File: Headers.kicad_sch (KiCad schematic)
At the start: 17 parts, among them J1 Conn_01x06_Pin, J10 Conn_01x03_Pin, J11 Conn_02x05_Odd_Even, J17 Conn_01x01_Pin, J18 Conn_02x05_Odd_Even, J2 Conn_01x06_Pin, J21 Conn_01x02_Pin, J5 Conn_01x02_Pin, J8 Conn_01x03_Pin

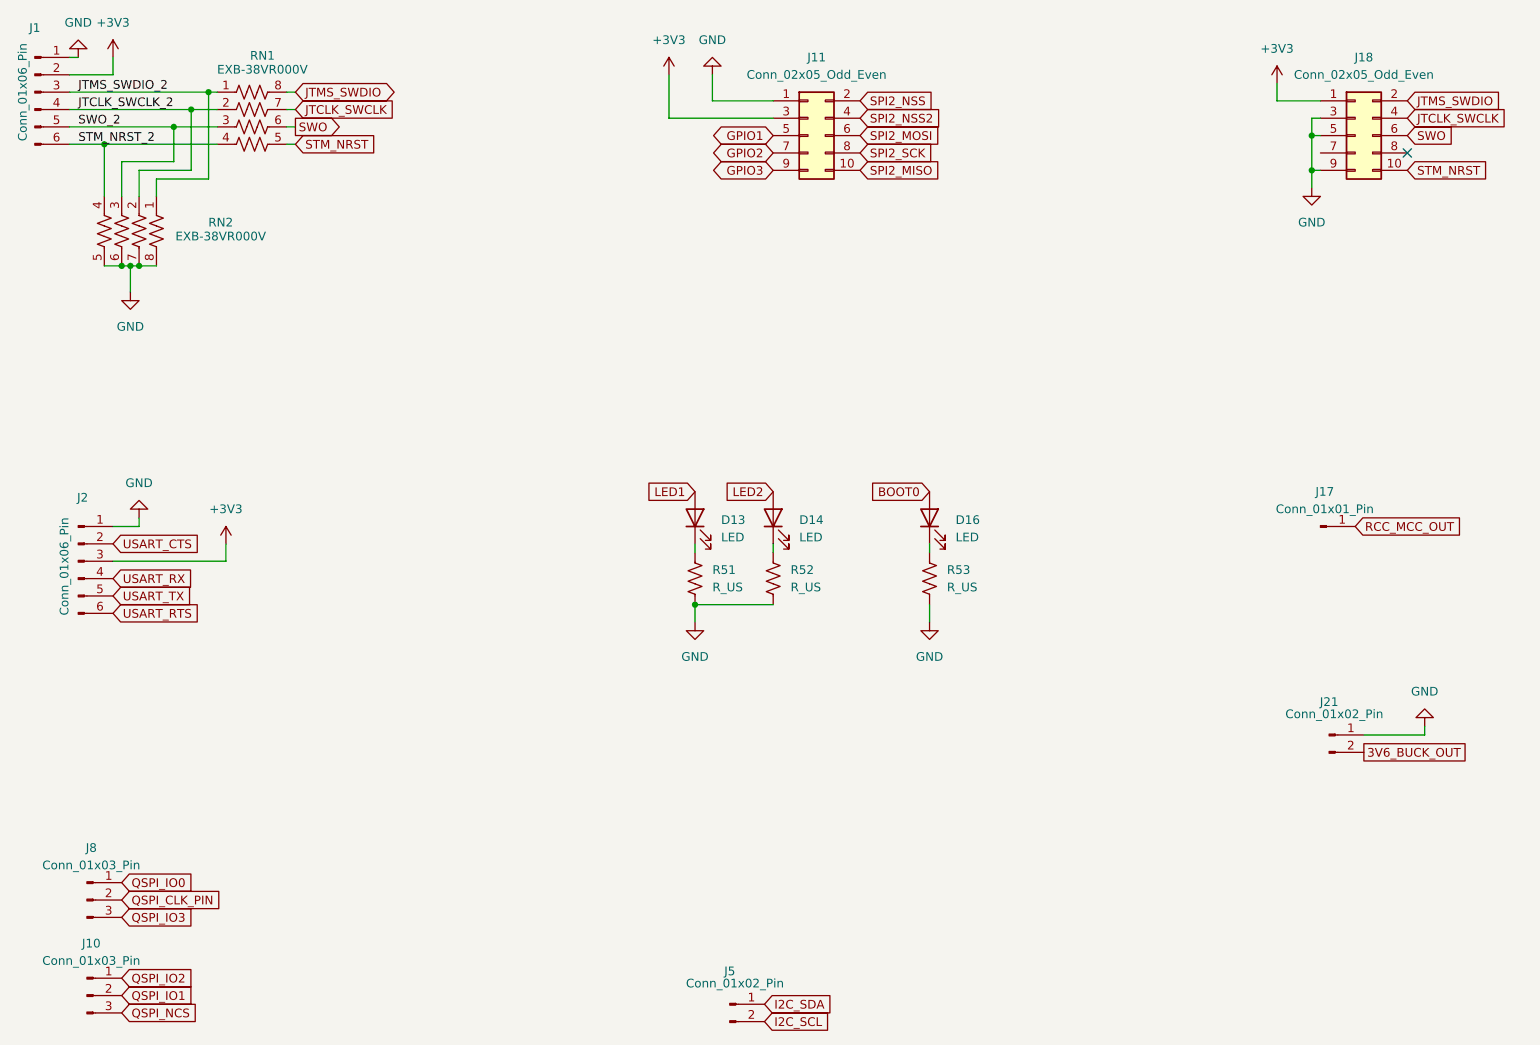
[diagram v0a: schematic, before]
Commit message: First draft of design output, schematic, and layout complete
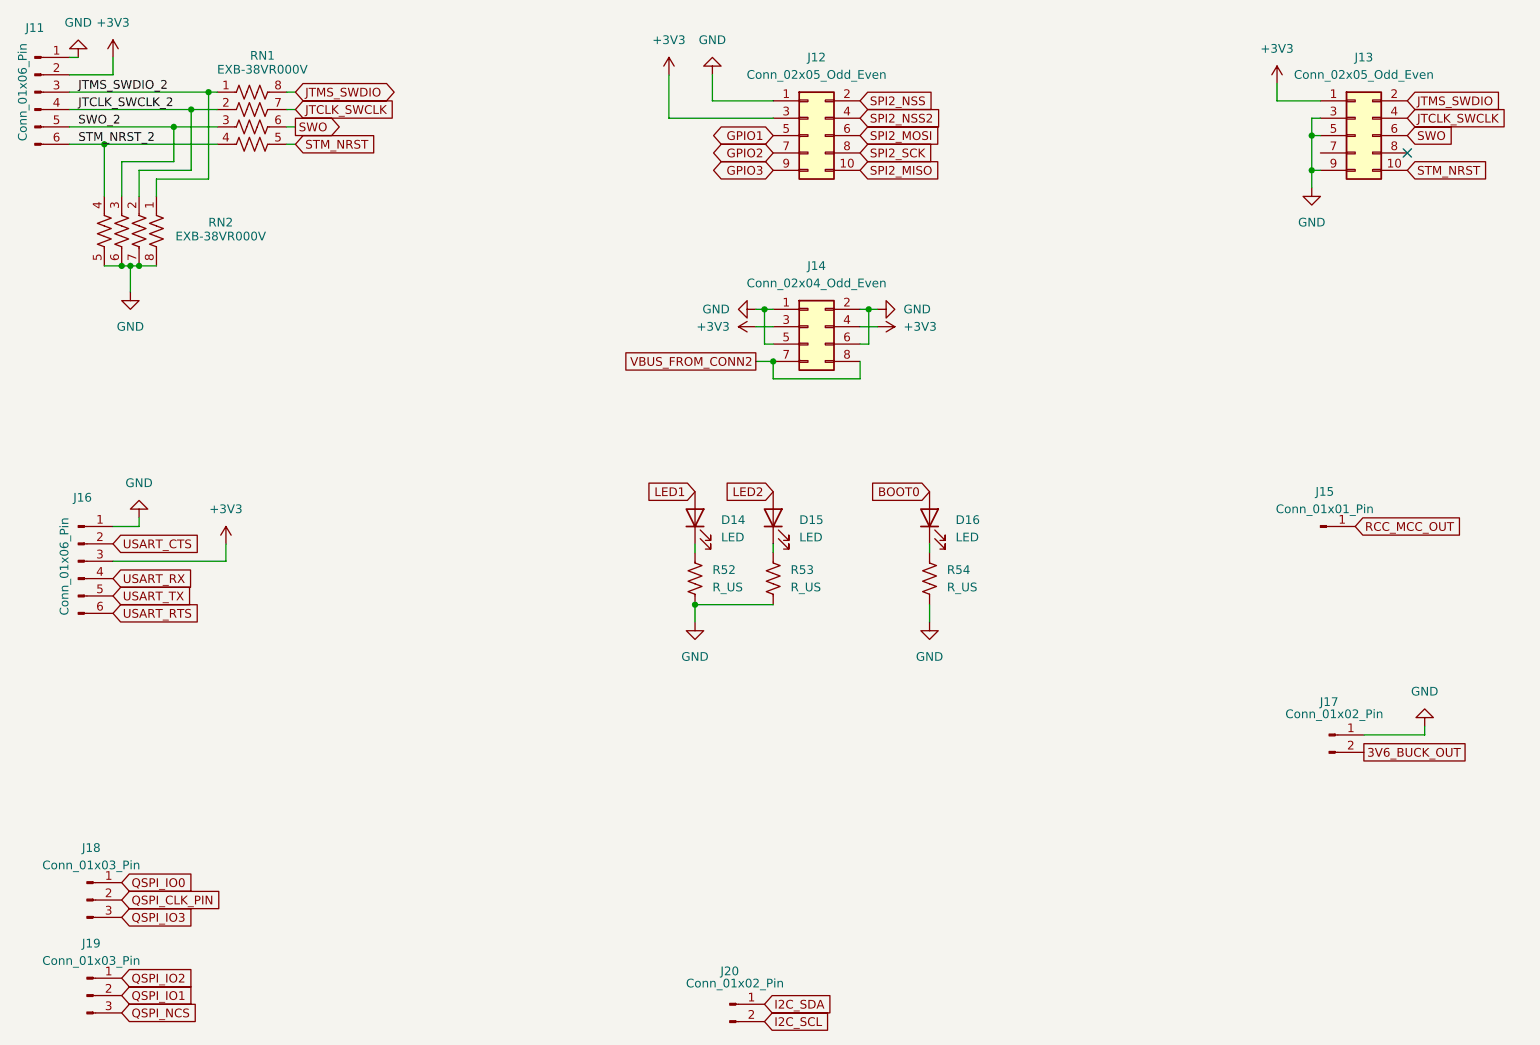
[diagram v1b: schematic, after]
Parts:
- added J14: Conn_02x04_Odd_Even, Connector_PinHeader_2.54mm:PinHeader_2x04_P2.54mm_Vertical, symbol Connector_Generic:Conn_02x04_Odd_Even
- renumbered D13 to D14, D14 to D15, J1 to J11, J11 to J12, J18 to J13, J17 to J15, J2 to J16, J21 to J17, J8 to J18, J10 to J19, J5 to J20, R51 to R52, R52 to R53, R53 to R54
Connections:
- net +3V3: now also J14.3 (Pin_3), J14.4 (Pin_4)
- net GND: now also J14.1 (Pin_1), J14.2 (Pin_2), J14.5 (Pin_5), J14.6 (Pin_6)
- new net VBUS_FROM_CONN2: J14.7 (Pin_7), J14.8 (Pin_8)
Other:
- company: (none) -> Jacob Kapala
